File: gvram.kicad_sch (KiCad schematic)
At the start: 8 parts

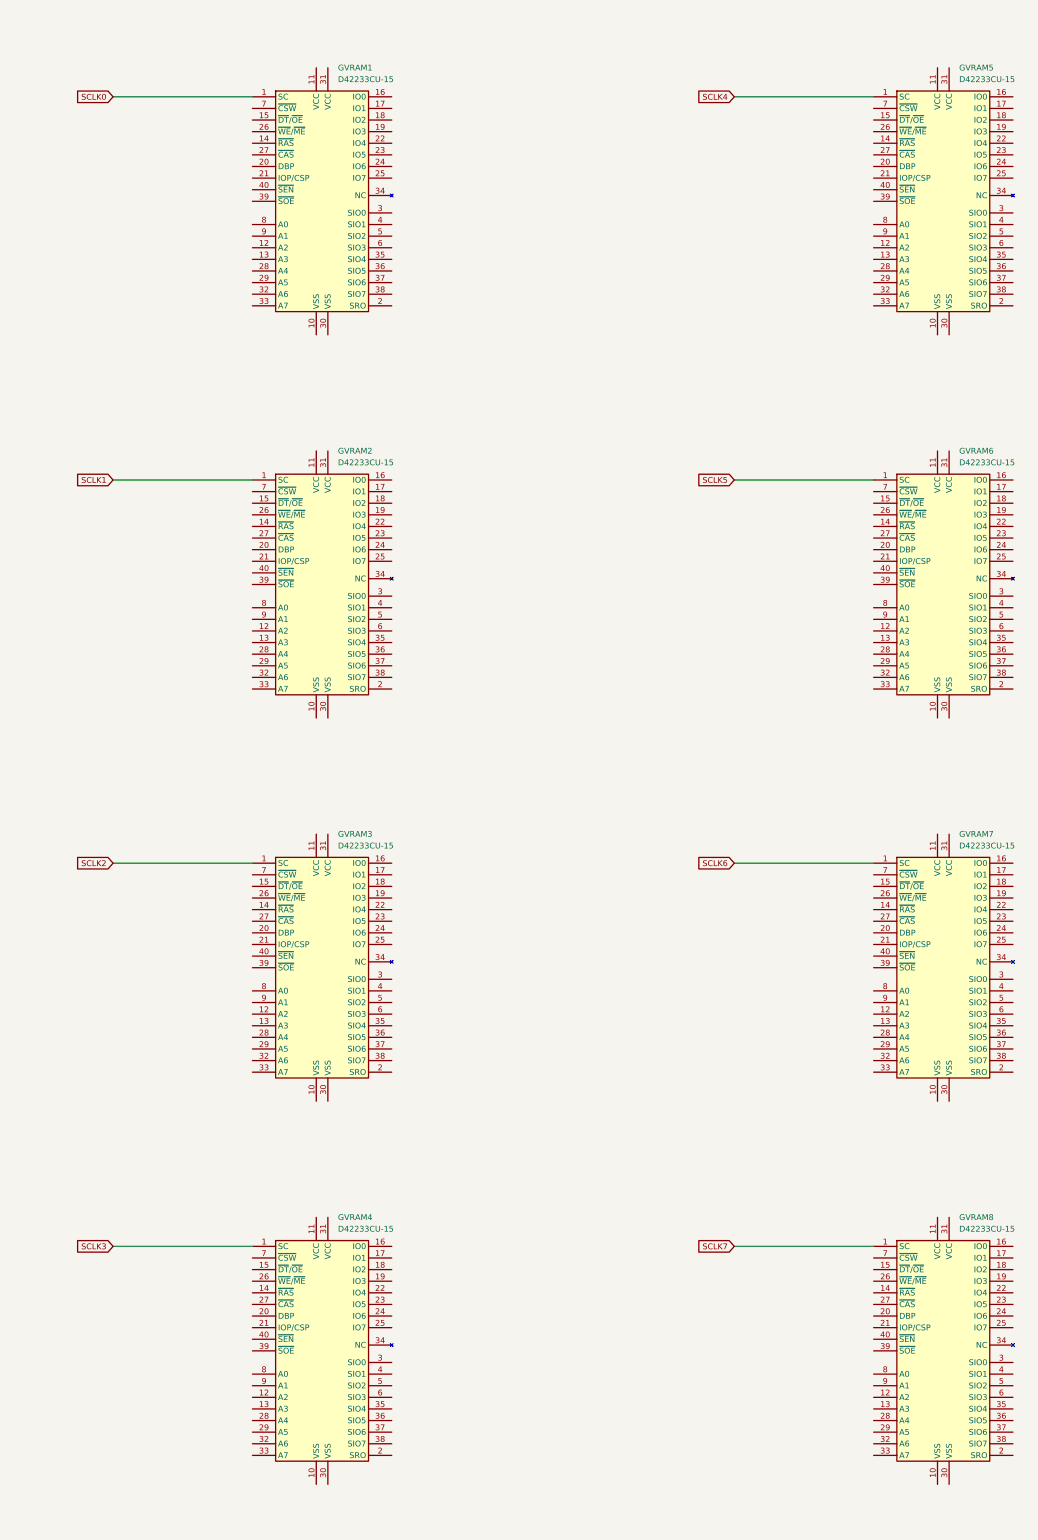
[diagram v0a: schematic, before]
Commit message: schematic: add lines between IC9 and GVRAM
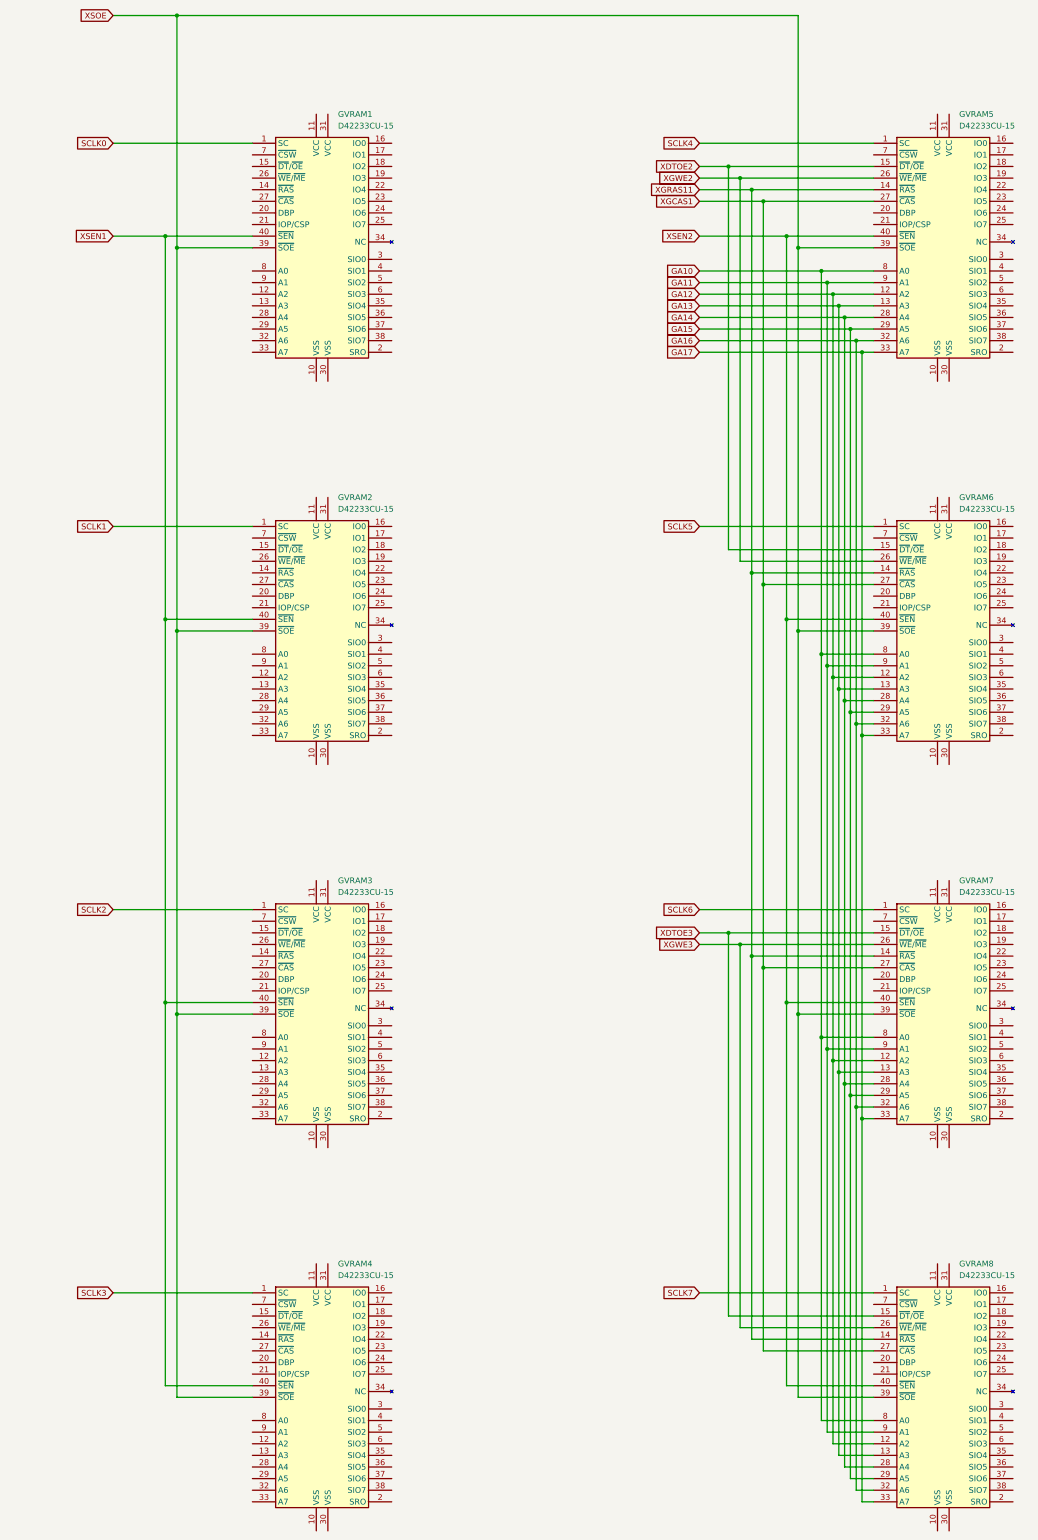
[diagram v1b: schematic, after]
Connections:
- net GA12: now reaches GVRAM8.12 (A2)
- net GA12: now also GVRAM5.12 (A2), GVRAM6.12 (A2), GVRAM7.12 (A2)
- net GA13: now reaches GVRAM8.13 (A3)
- net GA13: now also GVRAM5.13 (A3), GVRAM6.13 (A3), GVRAM7.13 (A3)
- net XGRAS11: now reaches GVRAM8.14 (~{RAS})
- net XGRAS11: now also GVRAM5.14 (~{RAS}), GVRAM6.14 (~{RAS}), GVRAM7.14 (~{RAS})
- net XDTOE3: now reaches GVRAM8.15 (~{DT}/~{OE})
- net XDTOE3: now also GVRAM7.15 (~{DT}/~{OE})
- net XGWE3: now reaches GVRAM8.26 (~{WE}/~{ME})
- net XGWE3: now also GVRAM7.26 (~{WE}/~{ME})
- net XGCAS1: now reaches GVRAM8.27 (~{CAS})
- net XGCAS1: now also GVRAM5.27 (~{CAS}), GVRAM6.27 (~{CAS}), GVRAM7.27 (~{CAS})
- net GA14: now reaches GVRAM8.28 (A4)
- net GA14: now also GVRAM5.28 (A4), GVRAM6.28 (A4), GVRAM7.28 (A4)
- net GA15: now reaches GVRAM8.29 (A5)
- net GA15: now also GVRAM5.29 (A5), GVRAM6.29 (A5), GVRAM7.29 (A5)
- net GA16: now reaches GVRAM8.32 (A6)
- net GA16: now also GVRAM5.32 (A6), GVRAM6.32 (A6), GVRAM7.32 (A6)
- net GA17: now reaches GVRAM8.33 (A7)
- net GA17: now also GVRAM5.33 (A7), GVRAM6.33 (A7), GVRAM7.33 (A7)
- net XSOE: now reaches GVRAM8.39 (~{SOE})
- net XSOE: now also GVRAM1.39 (~{SOE}), GVRAM2.39 (~{SOE}), GVRAM3.39 (~{SOE}), GVRAM4.39 (~{SOE}), GVRAM5.39 (~{SOE}), GVRAM6.39 (~{SOE}), GVRAM7.39 (~{SOE})
- net XSEN2: now reaches GVRAM8.40 (~{SEN})
- net XSEN2: now also GVRAM5.40 (~{SEN}), GVRAM6.40 (~{SEN}), GVRAM7.40 (~{SEN})
- net GA10: now reaches GVRAM8.8 (A0)
- net GA10: now also GVRAM5.8 (A0), GVRAM6.8 (A0), GVRAM7.8 (A0)
- net GA11: now reaches GVRAM8.9 (A1)
- net GA11: now also GVRAM5.9 (A1), GVRAM6.9 (A1), GVRAM7.9 (A1)
- net XDTOE2: now reaches GVRAM5.15 (~{DT}/~{OE})
- net XDTOE2: now also GVRAM6.15 (~{DT}/~{OE})
- net XGWE2: now reaches GVRAM5.26 (~{WE}/~{ME})
- net XGWE2: now also GVRAM6.26 (~{WE}/~{ME})
- net XSEN1: now reaches GVRAM4.40 (~{SEN})
- net XSEN1: now also GVRAM1.40 (~{SEN}), GVRAM2.40 (~{SEN}), GVRAM3.40 (~{SEN})
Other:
- moved on the sheet: GVRAM1, GVRAM2, GVRAM3, GVRAM4, GVRAM5, GVRAM6, GVRAM7, GVRAM8

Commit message: schematic: add lines from IC9 to GVRAM1-4
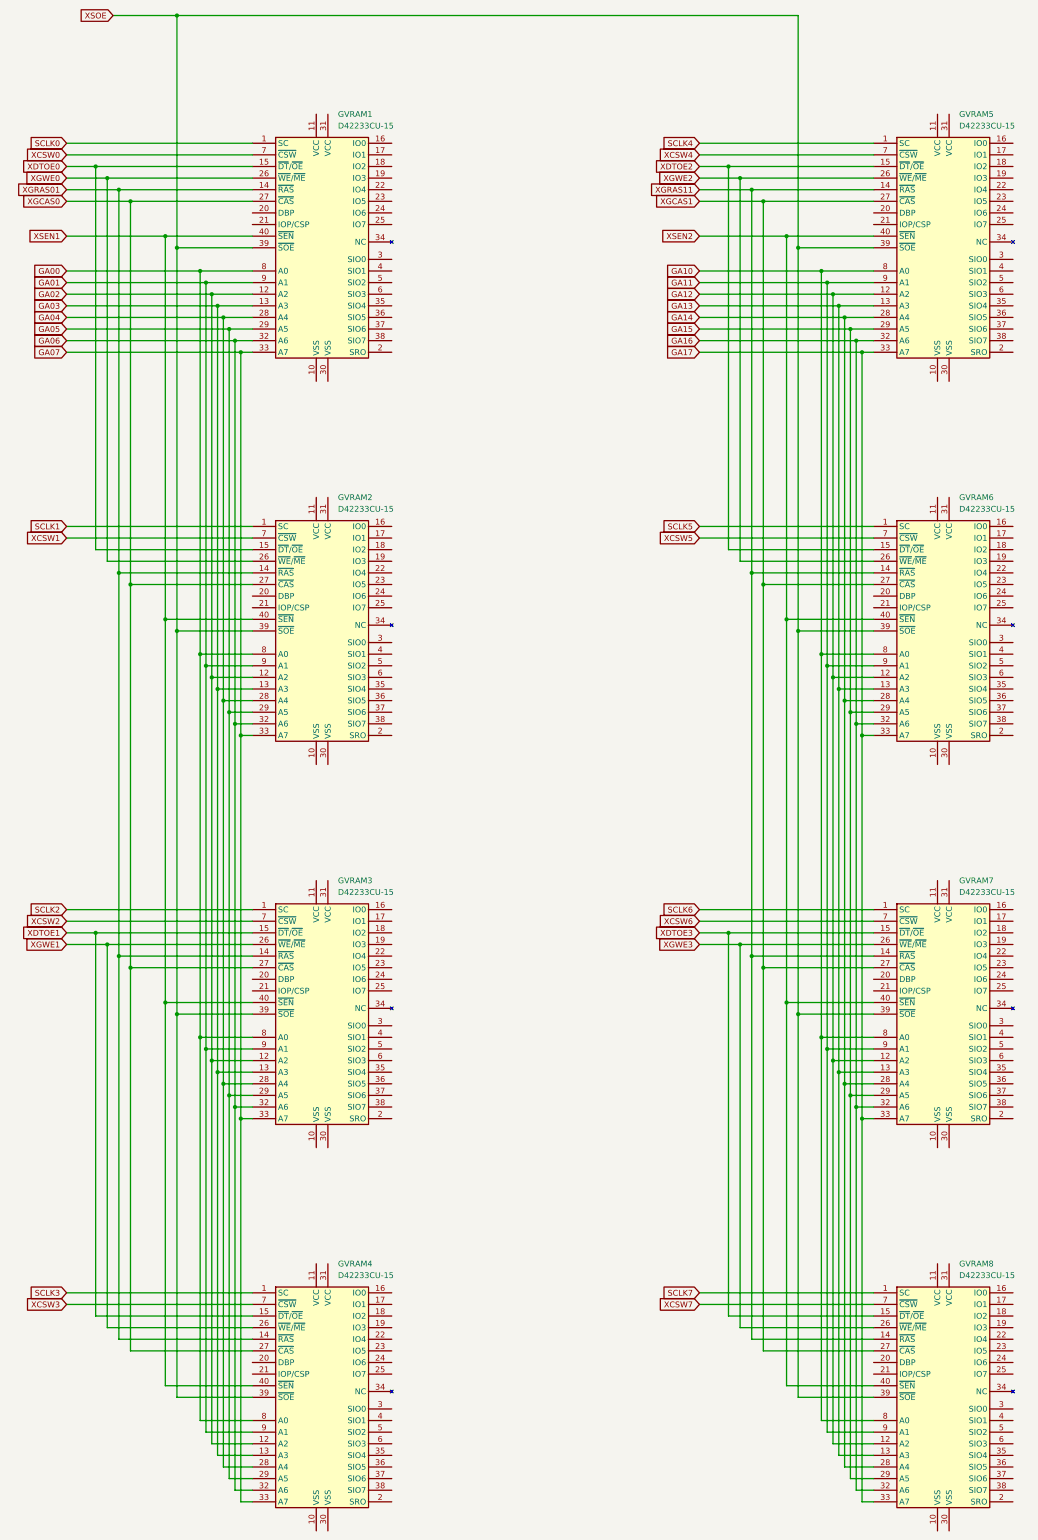
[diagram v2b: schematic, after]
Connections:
- net XCSW7: now reaches GVRAM8.7 (~{CSW})
- net XCSW4: now reaches GVRAM5.7 (~{CSW})
- net GA02: now reaches GVRAM4.12 (A2)
- net GA02: now also GVRAM1.12 (A2), GVRAM2.12 (A2), GVRAM3.12 (A2)
- net GA03: now reaches GVRAM4.13 (A3)
- net GA03: now also GVRAM1.13 (A3), GVRAM2.13 (A3), GVRAM3.13 (A3)
- net XGRAS01: now reaches GVRAM4.14 (~{RAS})
- net XGRAS01: now also GVRAM1.14 (~{RAS}), GVRAM2.14 (~{RAS}), GVRAM3.14 (~{RAS})
- net XDTOE1: now reaches GVRAM4.15 (~{DT}/~{OE})
- net XDTOE1: now also GVRAM3.15 (~{DT}/~{OE})
- net XGWE1: now reaches GVRAM4.26 (~{WE}/~{ME})
- net XGWE1: now also GVRAM3.26 (~{WE}/~{ME})
- net XGCAS0: now reaches GVRAM4.27 (~{CAS})
- net XGCAS0: now also GVRAM1.27 (~{CAS}), GVRAM2.27 (~{CAS}), GVRAM3.27 (~{CAS})
- net GA04: now reaches GVRAM4.28 (A4)
- net GA04: now also GVRAM1.28 (A4), GVRAM2.28 (A4), GVRAM3.28 (A4)
- net GA05: now reaches GVRAM4.29 (A5)
- net GA05: now also GVRAM1.29 (A5), GVRAM2.29 (A5), GVRAM3.29 (A5)
- net GA06: now reaches GVRAM4.32 (A6)
- net GA06: now also GVRAM1.32 (A6), GVRAM2.32 (A6), GVRAM3.32 (A6)
- net GA07: now reaches GVRAM4.33 (A7)
- net GA07: now also GVRAM1.33 (A7), GVRAM2.33 (A7), GVRAM3.33 (A7)
- net XCSW3: now reaches GVRAM4.7 (~{CSW})
- net GA00: now reaches GVRAM4.8 (A0)
- net GA00: now also GVRAM1.8 (A0), GVRAM2.8 (A0), GVRAM3.8 (A0)
- net GA01: now reaches GVRAM4.9 (A1)
- net GA01: now also GVRAM1.9 (A1), GVRAM2.9 (A1), GVRAM3.9 (A1)
- net XDTOE0: now reaches GVRAM1.15 (~{DT}/~{OE})
- net XDTOE0: now also GVRAM2.15 (~{DT}/~{OE})
- net XGWE0: now reaches GVRAM1.26 (~{WE}/~{ME})
- net XGWE0: now also GVRAM2.26 (~{WE}/~{ME})
- net XCSW0: now reaches GVRAM1.7 (~{CSW})
- net XCSW1: now reaches GVRAM2.7 (~{CSW})
- net XCSW6: now reaches GVRAM7.7 (~{CSW})
- net XCSW2: now reaches GVRAM3.7 (~{CSW})
- net XCSW5: now reaches GVRAM6.7 (~{CSW})

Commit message: schematic: tidy hierarchical sheets
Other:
- title: (none) -> グラフィックVRAM
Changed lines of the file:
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@@
   (paper "A3" portrait)
   (title_block
+    (title "グラフィックVRAM")
     (comment 1 "VA1回路図 P.258-259")
   )
